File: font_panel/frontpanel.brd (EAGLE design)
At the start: 97 x 40 mm, 20 parts

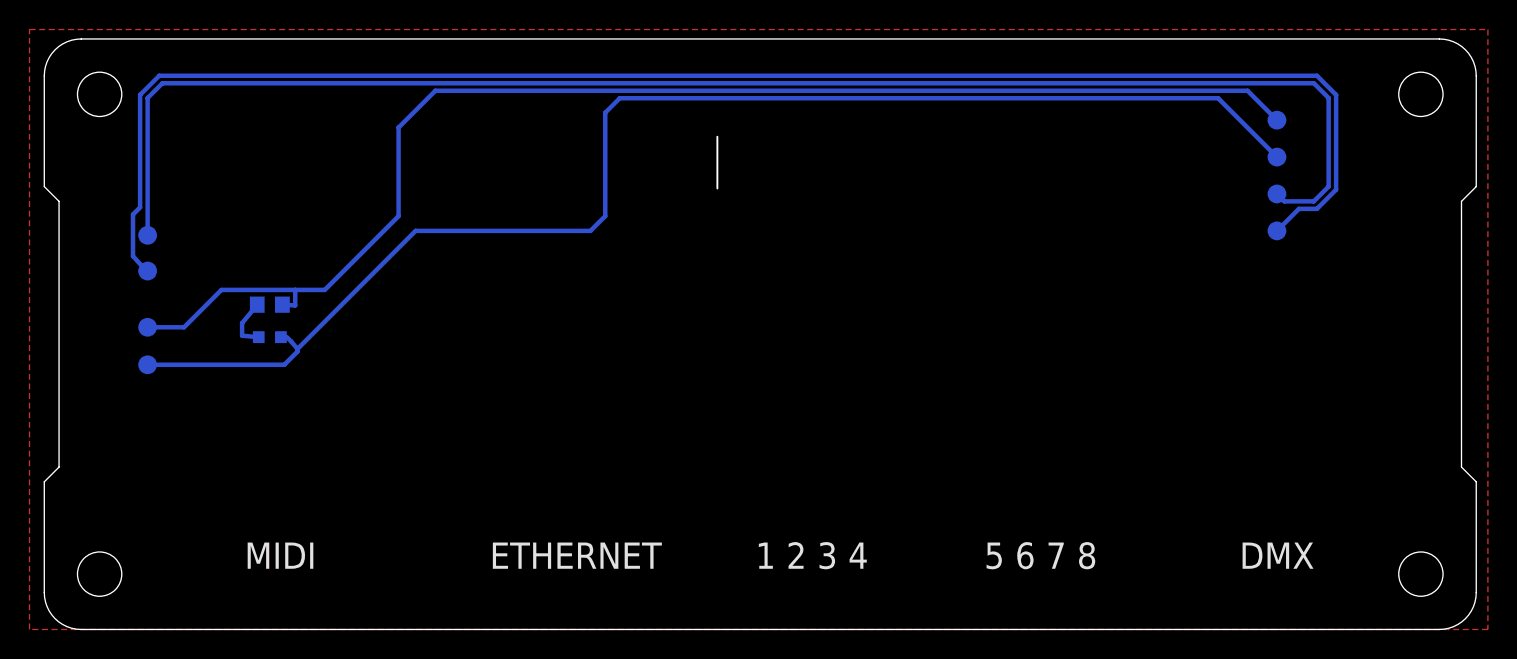
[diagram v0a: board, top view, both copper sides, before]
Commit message: front panel initial modifications
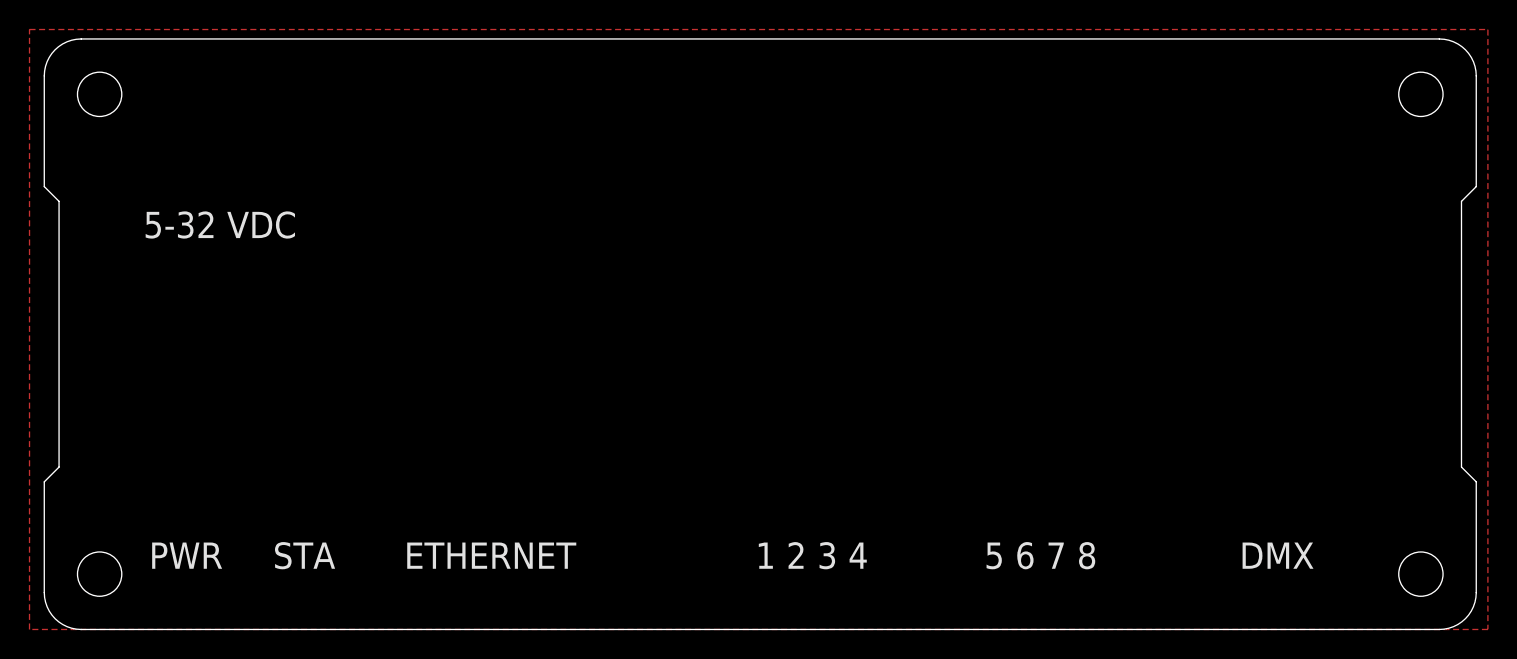
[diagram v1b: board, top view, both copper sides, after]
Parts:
- removed LED1: (no value), Multischriever:ADAFRUIT_CHIPLED_0603_REVERSE
- removed PAD_3V1, PAD_3V3, PAD_GND, PAD_GND1, PAD_SCL, PAD_SCL1, PAD_SDA, PAD_SDA1: TPB1,27, testpad:B1,27
- removed R1: (no value), Multischriever:ADAFRUIT_R0603
- removed U$10: HOLESOLED, Multischriever:OLDHOLE
- removed U$11: (no value), Multischriever:ANTENNAHOLE
- removed U$9: HOLESROTARY, Multischriever:ROTARYHOLE
- added U$2: HOLESLED_THROUGH_PCB, Multischriever:ADAFRUIT_CHIPLED_0603_REVERSE_NOLED
- U$8: value HOLESUSBA -> HOLESLED_THROUGH_PCB; device Multischriever:USBAHOLE -> Multischriever:ADAFRUIT_CHIPLED_0603_REVERSE_NOLED
- moved U$7 73.6 mm to (12.4, 31.6)
- moved U$1 23.6 mm to (11.9, 18.5)
- moved U$6 6.23 mm to (30.2, 9.25)
- moved U$8 2.42 mm to (17.6, 8.30)
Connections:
- removed net 3V3: LED1.A, PAD_3V1.TP, PAD_3V3.TP
- removed net GND: PAD_GND.TP, PAD_GND1.TP, R1.2
- removed net N$3: LED1.C, R1.1
- removed net SCL: PAD_SCL.TP, PAD_SCL1.TP
- removed net SDA: PAD_SDA.TP, PAD_SDA1.TP
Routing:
- net SDA: track 106.2 -> 0.00 mm
- net SCL: track 100.2 -> 0.00 mm
- net 3V3: track 90.9 -> 0.00 mm
- net GND: track 89.4 -> 0.00 mm
- net N$3: track 3.60 -> 0.00 mm
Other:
- board text added: "5-32 VDC"
- board text added: "HyperNode Front REVA"
- board text added: "PWR"
- board text added: "STA"
- board text removed: "3v3"
- board text removed: ">"
- board text removed: "Front REVD"
- board text removed: "GND"
- board text removed: "MIDI"
- board text removed: "SCL"
- board text removed: "SDA"

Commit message: measurements before origin move
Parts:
- moved U$8 3.20 mm to (14.4, 8.30)
- moved U$7 0.40 mm to (12.0, 31.6)
- moved U$1 0.10 mm to (12.0, 18.5)
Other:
- board text added: "P"
- board text added: "S"
- board text removed: "PWR"
- board text removed: "STA"
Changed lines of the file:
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@@
 <setting verticaltext="up"/>
 </settings>
-<grid distance="1.6" unitdist="mm" unit="mm" style="lines" multiple="1" display="yes" altdistance="0.1" altunitdist="mm" altunit="mm"/>
+<grid distance="1.6" unitdist="mm" unit="mm" style="lines" multiple="1" display="yes" altdistance="1" altunitdist="mm" altunit="mm"/>
 <layers>
 <layer number="1" name="Top" color="4" fill="1" visible="yes" active="yes"/>
@@
 <rectangle x1="91" y1="0" x2="97" y2="6" layer="40"/>
 <rectangle x1="91" y1="34" x2="97" y2="40" layer="40"/>
-<text x="83.5" y="5" size="1.778" layer="121" align="center">DMX</text>
-<text x="52" y="5" size="1.778" layer="121" align="center">1 2 3 4</text>
-<text x="67.5" y="5" size="1.778" layer="121" align="center">5 6 7 8</text>
+<text x="82.7" y="5" size="1.778" layer="121" align="center">DMX</text>
+<text x="51.697" y="5" size="1.778" layer="121" align="center">1 2 3 4</text>
+<text x="67.44" y="5" size="1.778" layer="121" align="center">5 6 7 8</text>
 <text x="30.2" y="5" size="1.778" layer="121" align="center">ETHERNET</text>
 <text x="93" y="21" size="1.778" layer="122" rot="MR90" align="center">JLCJLCJLCJLC</text>
 <text x="95" y="21" size="1.778" layer="122" rot="MR90" align="center">HyperNode Front REVA</text>
 <dimension x1="35.2" y1="7.6" x2="35.2" y2="9.2" x3="33.6" y3="8.4" textsize="0.8128" layer="47"/>
-<dimension x1="91.2" y1="11.2" x2="17.6" y2="11.2" x3="54.4" y3="-6.4" textsize="0.8128" layer="47"/>
+<dimension x1="91.2" y1="11.2" x2="14.4" y2="11.2" x3="52.8" y3="-6.4" textsize="0.8128" layer="47"/>
 <dimension x1="91.2" y1="11.2" x2="9.6" y2="11.2" x3="50.4" y3="-9.6" textsize="0.8128" layer="47"/>
 <dimension x1="43.2" y1="9.6" x2="38.6" y2="9.6" x3="40.9" y3="-3.2" textsize="0.8128" layer="47"/>
-<text x="9.6" y="5" size="1.778" layer="121" align="center">PWR</text>
-<text x="11.9" y="27.4" size="1.778" layer="121" align="center">5-32 VDC</text>
-<text x="17.6" y="5" size="1.778" layer="121" align="center">STA</text>
+<text x="9.6" y="5" size="1.778" layer="121" align="center">P</text>
+<text x="12" y="25.8" size="1.778" layer="121" align="center">5-32 VDC</text>
+<text x="14.4" y="5" size="1.778" layer="121" align="center">S</text>
+<dimension x1="0" y1="40" x2="97" y2="40" x3="48.5" y3="41.6" textsize="0.8128" layer="47"/>
+<dimension x1="9.6" y1="8.3" x2="0" y2="8" x3="4.8" y3="-3.2" textsize="0.8128" layer="47" dtype="horizontal"/>
+<dimension x1="14.4" y1="8.3" x2="0" y2="8" x3="7.2" y3="-4.8" textsize="0.8128" layer="47" dtype="horizontal"/>
+<dimension x1="30.2" y1="9.25" x2="0" y2="-14.4" x3="15.1" y3="-6.4" textsize="0.8128" layer="47" dtype="horizontal"/>
+<dimension x1="43.2" y1="9.6" x2="0" y2="9.6" x3="21.6" y3="-8" textsize="0.8128" layer="47" dtype="horizontal"/>
+<dimension x1="91.2" y1="11.2" x2="0" y2="9.6" x3="45.6" y3="-11.2" textsize="0.8128" layer="47" dtype="horizontal"/>
 </plain>
 <attributes>
@@
 </autorouter>
 <elements>
-<element name="U$1" library="Multischriever" package="DCBARREL2.1" value="HOLESDCBARREL2.1" x="11.9" y="18.5" smashed="yes" rot="R90"/>
+<element name="U$1" library="Multischriever" package="DCBARREL2.1" value="HOLESDCBARREL2.1" x="12" y="18.5" smashed="yes" rot="R90"/>
 <element name="U$3" library="Multischriever" package="RJ45HOLE_NOSHIELD" value="HOLESRJ45_NOSHIELD" x="82.7" y="7.6" smashed="yes"/>
 <element name="U$4" library="Multischriever" package="RJ45HOLE_NOSHIELD" value="HOLESRJ45_NOSHIELD" x="67.44" y="7.6" smashed="yes"/>
 <element name="U$5" library="Multischriever" package="RJ45HOLE_NOSHIELD" value="HOLESRJ45_NOSHIELD" x="51.697" y="7.6" smashed="yes"/>
 <element name="U$6" library="Multischriever" package="RJ45HOLE" value="HOLESRJ45" x="30.2" y="9.25" smashed="yes"/>
-<element name="U$7" library="Multischriever" package="MULTISCHRIEVERLOGO_SOLDERMASK" value="" x="12.4" y="31.6" smashed="yes"/>
+<element name="U$7" library="Multischriever" package="MULTISCHRIEVERLOGO_SOLDERMASK" value="" x="12" y="31.6" smashed="yes"/>
 <element name="U$2" library="Multischriever" package="ADAFRUIT_CHIPLED_0603_REVERSE_NOLED" value="HOLESLED_THROUGH_PCB" x="9.6" y="8.3" smashed="yes"/>
-<element name="U$8" library="Multischriever" package="ADAFRUIT_CHIPLED_0603_REVERSE_NOLED" value="HOLESLED_THROUGH_PCB" x="17.6" y="8.3" smashed="yes"/>
+<element name="U$8" library="Multischriever" package="ADAFRUIT_CHIPLED_0603_REVERSE_NOLED" value="HOLESLED_THROUGH_PCB" x="14.4" y="8.3" smashed="yes"/>
 </elements>
 <signals>

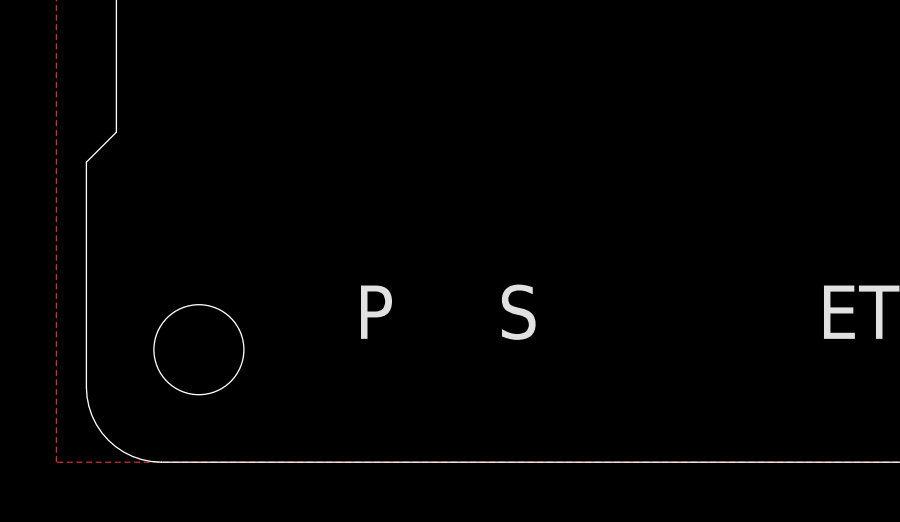
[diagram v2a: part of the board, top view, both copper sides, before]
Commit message: align front panel
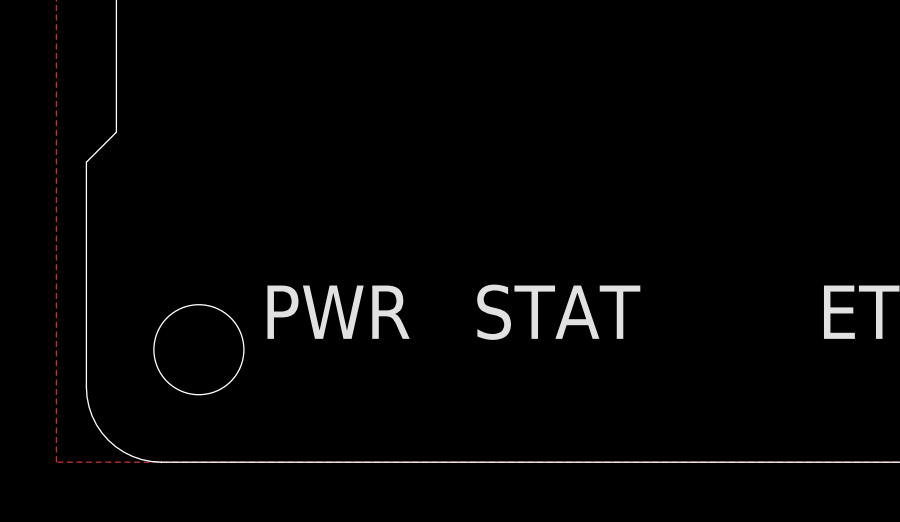
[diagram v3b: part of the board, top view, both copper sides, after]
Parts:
- moved U$2 1.27 mm to (8.33, 8.30)
- moved U$8 1.27 mm to (15.7, 8.30)
- moved U$6 1.01 mm to (31.2, 9.25)
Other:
- board text added: "PWR"
- board text added: "STAT"
- board text removed: "P"
- board text removed: "S"
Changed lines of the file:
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@@
 <text x="95" y="21" size="1.778" layer="122" rot="MR90" align="center">HyperNode Front REVA</text>
 <dimension x1="35.2" y1="7.6" x2="35.2" y2="9.2" x3="33.6" y3="8.4" textsize="0.8128" layer="47"/>
-<dimension x1="91.2" y1="11.2" x2="14.4" y2="11.2" x3="52.8" y3="-6.4" textsize="0.8128" layer="47"/>
-<dimension x1="91.2" y1="11.2" x2="9.6" y2="11.2" x3="50.4" y3="-9.6" textsize="0.8128" layer="47"/>
-<dimension x1="43.2" y1="9.6" x2="38.6" y2="9.6" x3="40.9" y3="-3.2" textsize="0.8128" layer="47"/>
-<text x="9.6" y="5" size="1.778" layer="121" align="center">P</text>
+<text x="8.33" y="5" size="1.778" layer="121" align="center">PWR</text>
 <text x="12" y="25.8" size="1.778" layer="121" align="center">5-32 VDC</text>
-<text x="14.4" y="5" size="1.778" layer="121" align="center">S</text>
+<text x="15.67" y="5" size="1.778" layer="121" align="center">STAT</text>
 <dimension x1="0" y1="40" x2="97" y2="40" x3="48.5" y3="41.6" textsize="0.8128" layer="47"/>
-<dimension x1="9.6" y1="8.3" x2="0" y2="8" x3="4.8" y3="-3.2" textsize="0.8128" layer="47" dtype="horizontal"/>
-<dimension x1="14.4" y1="8.3" x2="0" y2="8" x3="7.2" y3="-4.8" textsize="0.8128" layer="47" dtype="horizontal"/>
-<dimension x1="30.2" y1="9.25" x2="0" y2="-14.4" x3="15.1" y3="-6.4" textsize="0.8128" layer="47" dtype="horizontal"/>
-<dimension x1="43.2" y1="9.6" x2="0" y2="9.6" x3="21.6" y3="-8" textsize="0.8128" layer="47" dtype="horizontal"/>
-<dimension x1="91.2" y1="11.2" x2="0" y2="9.6" x3="45.6" y3="-11.2" textsize="0.8128" layer="47" dtype="horizontal"/>
+<dimension x1="8.33" y1="8.3" x2="0" y2="8" x3="4.165" y3="-3.2" textsize="0.8128" layer="47" dtype="horizontal"/>
+<dimension x1="15.67" y1="8.3" x2="0" y2="8" x3="7.835" y3="-4.8" textsize="0.8128" layer="47" dtype="horizontal"/>
+<dimension x1="31.21" y1="9.25" x2="0" y2="-14.4" x3="15.605" y3="-6.4" textsize="0.8128" layer="47" dtype="horizontal"/>
+<dimension x1="43.82" y1="9.6" x2="0" y2="9.6" x3="21.91" y3="-8" textsize="0.8128" layer="47" dtype="horizontal"/>
+<dimension x1="90.81" y1="9.6" x2="0" y2="0" x3="45.405" y3="-9.6" textsize="0.8128" layer="47" dtype="horizontal"/>
 </plain>
 <attributes>
@@
 <element name="U$4" library="Multischriever" package="RJ45HOLE_NOSHIELD" value="HOLESRJ45_NOSHIELD" x="67.44" y="7.6" smashed="yes"/>
 <element name="U$5" library="Multischriever" package="RJ45HOLE_NOSHIELD" value="HOLESRJ45_NOSHIELD" x="51.697" y="7.6" smashed="yes"/>
-<element name="U$6" library="Multischriever" package="RJ45HOLE" value="HOLESRJ45" x="30.2" y="9.25" smashed="yes"/>
+<element name="U$6" library="Multischriever" package="RJ45HOLE" value="HOLESRJ45" x="31.21" y="9.25" smashed="yes"/>
 <element name="U$7" library="Multischriever" package="MULTISCHRIEVERLOGO_SOLDERMASK" value="" x="12" y="31.6" smashed="yes"/>
-<element name="U$2" library="Multischriever" package="ADAFRUIT_CHIPLED_0603_REVERSE_NOLED" value="HOLESLED_THROUGH_PCB" x="9.6" y="8.3" smashed="yes"/>
-<element name="U$8" library="Multischriever" package="ADAFRUIT_CHIPLED_0603_REVERSE_NOLED" value="HOLESLED_THROUGH_PCB" x="14.4" y="8.3" smashed="yes"/>
+<element name="U$2" library="Multischriever" package="ADAFRUIT_CHIPLED_0603_REVERSE_NOLED" value="HOLESLED_THROUGH_PCB" x="8.33" y="8.3" smashed="yes"/>
+<element name="U$8" library="Multischriever" package="ADAFRUIT_CHIPLED_0603_REVERSE_NOLED" value="HOLESLED_THROUGH_PCB" x="15.67" y="8.3" smashed="yes"/>
 </elements>
 <signals>

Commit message: rev A
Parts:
- moved U$7 0.80 mm to (12.0, 32.4)
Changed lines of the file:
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@@
 <setting verticaltext="up"/>
 </settings>
-<grid distance="1.6" unitdist="mm" unit="mm" style="lines" multiple="1" display="yes" altdistance="1" altunitdist="mm" altunit="mm"/>
+<grid distance="1.6" unitdist="mm" unit="mm" style="lines" multiple="1" display="yes" altdistance="0.8" altunitdist="mm" altunit="mm"/>
 <layers>
 <layer number="1" name="Top" color="4" fill="1" visible="yes" active="yes"/>
@@
 <dimension x1="35.2" y1="7.6" x2="35.2" y2="9.2" x3="33.6" y3="8.4" textsize="0.8128" layer="47"/>
 <text x="8.33" y="5" size="1.778" layer="121" align="center">PWR</text>
-<text x="12" y="25.8" size="1.778" layer="121" align="center">5-32 VDC</text>
+<text x="12" y="26.6" size="1.778" layer="121" align="center">5-32 VDC</text>
 <text x="15.67" y="5" size="1.778" layer="121" align="center">STAT</text>
 <dimension x1="0" y1="40" x2="97" y2="40" x3="48.5" y3="41.6" textsize="0.8128" layer="47"/>
@@
 <element name="U$5" library="Multischriever" package="RJ45HOLE_NOSHIELD" value="HOLESRJ45_NOSHIELD" x="51.697" y="7.6" smashed="yes"/>
 <element name="U$6" library="Multischriever" package="RJ45HOLE" value="HOLESRJ45" x="31.21" y="9.25" smashed="yes"/>
-<element name="U$7" library="Multischriever" package="MULTISCHRIEVERLOGO_SOLDERMASK" value="" x="12" y="31.6" smashed="yes"/>
+<element name="U$7" library="Multischriever" package="MULTISCHRIEVERLOGO_SOLDERMASK" value="" x="12" y="32.4" smashed="yes"/>
 <element name="U$2" library="Multischriever" package="ADAFRUIT_CHIPLED_0603_REVERSE_NOLED" value="HOLESLED_THROUGH_PCB" x="8.33" y="8.3" smashed="yes"/>
 <element name="U$8" library="Multischriever" package="ADAFRUIT_CHIPLED_0603_REVERSE_NOLED" value="HOLESLED_THROUGH_PCB" x="15.67" y="8.3" smashed="yes"/>

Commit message: move wrt32 away from ws2812 ports
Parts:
- moved U$6 0.64 mm to (30.6, 9.25)
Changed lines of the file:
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@@
 <setting verticaltext="up"/>
 </settings>
-<grid distance="1.6" unitdist="mm" unit="mm" style="lines" multiple="1" display="yes" altdistance="0.8" altunitdist="mm" altunit="mm"/>
+<grid distance="25" unitdist="mil" unit="mil" style="lines" multiple="1" display="yes" altdistance="6.25" altunitdist="mm" altunit="mm"/>
 <layers>
 <layer number="1" name="Top" color="4" fill="1" visible="yes" active="yes"/>
@@
 <dimension x1="8.33" y1="8.3" x2="0" y2="8" x3="4.165" y3="-3.2" textsize="0.8128" layer="47" dtype="horizontal"/>
 <dimension x1="15.67" y1="8.3" x2="0" y2="8" x3="7.835" y3="-4.8" textsize="0.8128" layer="47" dtype="horizontal"/>
-<dimension x1="31.21" y1="9.25" x2="0" y2="-14.4" x3="15.605" y3="-6.4" textsize="0.8128" layer="47" dtype="horizontal"/>
+<dimension x1="30.575" y1="9.25" x2="0" y2="-14.4" x3="15.2875" y3="-6.4" textsize="0.8128" layer="47" dtype="horizontal"/>
 <dimension x1="43.82" y1="9.6" x2="0" y2="9.6" x3="21.91" y3="-8" textsize="0.8128" layer="47" dtype="horizontal"/>
 <dimension x1="90.81" y1="9.6" x2="0" y2="0" x3="45.405" y3="-9.6" textsize="0.8128" layer="47" dtype="horizontal"/>
@@
 <element name="U$4" library="Multischriever" package="RJ45HOLE_NOSHIELD" value="HOLESRJ45_NOSHIELD" x="67.44" y="7.6" smashed="yes"/>
 <element name="U$5" library="Multischriever" package="RJ45HOLE_NOSHIELD" value="HOLESRJ45_NOSHIELD" x="51.697" y="7.6" smashed="yes"/>
-<element name="U$6" library="Multischriever" package="RJ45HOLE" value="HOLESRJ45" x="31.21" y="9.25" smashed="yes"/>
+<element name="U$6" library="Multischriever" package="RJ45HOLE" value="HOLESRJ45" x="30.575" y="9.25" smashed="yes"/>
 <element name="U$7" library="Multischriever" package="MULTISCHRIEVERLOGO_SOLDERMASK" value="" x="12" y="32.4" smashed="yes"/>
 <element name="U$2" library="Multischriever" package="ADAFRUIT_CHIPLED_0603_REVERSE_NOLED" value="HOLESLED_THROUGH_PCB" x="8.33" y="8.3" smashed="yes"/>
